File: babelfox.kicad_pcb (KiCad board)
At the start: 4 copper layers, 85.1 x 56 mm, 43 parts, among them J1 DCIN, J2 Battery, J3 GPIO, J4 Qwiic, J5 RJ45_Bel_SI-60062-F, J6 LoRA 900 SMA, J7 LoRA 2.4G ANT, J8 Cellular Ant, J9 LoRA 900 u.FL, Q1 FZ788B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

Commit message: board cleanup, add images
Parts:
- moved R9 6.23 mm to (160.6, 79.8), turned to -90 degrees
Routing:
- net BAT_Vcc: track 54.1 -> 64.1 mm
- net ADC1: track 11.6 -> 15.4 mm
- net 3v3: track 9.68 -> 12.4 mm
- net GND: vias 23 -> 24
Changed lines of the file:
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@@
 	(footprint "Resistor_SMD:R_0805_2012Metric_Pad1.20x1.40mm_HandSolder"
 		(layer "F.Cu")
-		(at 164.1856 84.8868 90)
+		(at 160.6296 79.772 -90)
 		(descr "Resistor SMD 0805 (2012 Metric), square (rectangular) end terminal, IPC_7351 nominal with elongated pad for handsoldering. (Body size source: IPC-SM-782 page 72, https://www.pcb-3d.com/wordpress/wp-content/uploads/ipc-sm-782a_amendment_1_and_2.pdf), generated with kicad-footprint-generator")
 		(tags "resistor handsolder")
 		(property "Reference" "R9"
-			(at 2.4892 0 180)
+			(at -2.5052 -0.0508 360)
 			(layer "F.SilkS")
 			(effects
@@
 		)
 		(property "Footprint" "Resistor_SMD:R_0805_2012Metric_Pad1.20x1.40mm_HandSolder"
-			(at 0 0 90)
+			(at 0 0 -90)
 			(unlocked yes)
 			(layer "F.Fab")
@@
 		)
 		(property "Datasheet" ""
-			(at 0 0 90)
+			(at 0 0 -90)
 			(unlocked yes)
 			(layer "F.Fab")
@@
 		)
 		(property "Description" "Resistor"
-			(at 0 0 90)
+			(at 0 0 -90)
 			(unlocked yes)
 			(layer "F.Fab")
@@
 		(attr smd)
 		(fp_line
-			(start -0.227064 -0.735)
-			(end 0.227064 -0.735)
+			(start -0.227064 0.735)
+			(end 0.227064 0.735)
 			(stroke
 				(width 0.12)
@@
 		)
 		(fp_line
-			(start -0.227064 0.735)
-			(end 0.227064 0.735)
+			(start -0.227064 -0.735)
+			(end 0.227064 -0.735)
 			(stroke
 				(width 0.12)
@@
 		)
 		(fp_line
-			(start 1.85 -0.95)
-			(end 1.85 0.95)
+			(start -1.85 0.95)
+			(end -1.85 -0.95)
 			(stroke
 				(width 0.05)
@@
 		)
 		(fp_line
-			(start -1.85 -0.95)
-			(end 1.85 -0.95)
+			(start 1.85 0.95)
+			(end -1.85 0.95)
 			(stroke
 				(width 0.05)
@@
 		)
 		(fp_line
-			(start 1.85 0.95)
-			(end -1.85 0.95)
+			(start -1.85 -0.95)
+			(end 1.85 -0.95)
 			(stroke
 				(width 0.05)
@@
 		)
 		(fp_line
-			(start -1.85 0.95)
-			(end -1.85 -0.95)
+			(start 1.85 -0.95)
+			(end 1.85 0.95)
 			(stroke
 				(width 0.05)
@@
 		)
 		(fp_line
-			(start 1 -0.625)
-			(end 1 0.625)
+			(start -1 0.625)
+			(end -1 -0.625)
 			(stroke
 				(width 0.1)
@@
 		)
 		(fp_line
-			(start -1 -0.625)
-			(end 1 -0.625)
+			(start 1 0.625)
+			(end -1 0.625)
 			(stroke
 				(width 0.1)
@@
 		)
 		(fp_line
-			(start 1 0.625)
-			(end -1 0.625)
+			(start -1 -0.625)
+			(end 1 -0.625)
 			(stroke
 				(width 0.1)
@@
 		)
 		(fp_line
-			(start -1 0.625)
-			(end -1 -0.625)
+			(start 1 -0.625)
+			(end 1 0.625)
 			(stroke
 				(width 0.1)
@@
 		)
 		(pad "1" smd roundrect
-			(at -1 0 90)
+			(at -1 0 270)
 			(size 1.2 1.4)
 			(layers "F.Cu" "F.Paste" "F.Mask")
@@
 		)
 		(pad "2" smd roundrect
-			(at 1 0 90)
+			(at 1 0 270)
 			(size 1.2 1.4)
 			(layers "F.Cu" "F.Paste" "F.Mask")
@@
 	)
 	(via
+		(at 163.2712 103.7336)
+		(size 0.6)
+		(drill 0.3)
+		(layers "F.Cu" "B.Cu")
+		(free yes)
+		(net 2)
+	)
+	(via
 		(at 175.8188 103.5812)
 		(size 0.6)
@@
 	)
 	(segment
+		(start 115.083 97.8408)
+		(end 116.4629 97.8408)
+		(width 0.4)
+		(layer "F.Cu")
+		(net 3)
+	)
+	(segment
 		(start 162.7124 115.9444)
 		(end 161.3728 115.9444)
@@
 	)
 	(segment
+		(start 116.4629 97.8408)
+		(end 116.6153 97.9932)
+		(width 0.4)
+		(layer "F.Cu")
+		(net 3)
+	)
+	(segment
 		(start 150.368 83.2104)
 		(end 150.368 83.1988)
@@
 		(net 3)
 	)
+	(segment
+		(start 116.5744 95.6564)
+		(end 117.6744 95.6564)
+		(width 0.4)
+		(layer "F.Cu")
+		(net 3)
+	)
 	(via
 		(at 154.7368 128.1176)
@@
 	)
 	(segment
-		(start 164.3032 86.0044)
-		(end 164.1856 85.8868)
-		(width 0.2)
-		(layer "F.Cu")
-		(net 4)
-	)
-	(segment
 		(start 168.830999 92.992201)
 		(end 168.656 93.1672)
@@
 	)
 	(segment
-		(start 165.4048 86.0044)
-		(end 164.3032 86.0044)
+		(start 161.258 78.772)
+		(end 162.1028 77.9272)
+		(width 0.2)
+		(layer "F.Cu")
+		(net 4)
+	)
+	(segment
+		(start 160.6296 78.772)
+		(end 161.258 78.772)
 		(width 0.2)
 		(layer "F.Cu")
@@
 	)
 	(via
-		(at 165.4048 86.0044)
+		(at 162.1028 77.9272)
 		(size 0.6)
 		(drill 0.3)
@@
 	)
 	(segment
-		(start 166.1682 86.0044)
-		(end 165.4048 86.0044)
+		(start 161.623327 81.459527)
+		(end 167.1842 87.0204)
 		(width 0.2)
 		(layer "B.Cu")
@@
 	)
 	(segment
+		(start 162.1028 77.9272)
+		(end 161.623327 78.406673)
+		(width 0.2)
+		(layer "B.Cu")
+		(net 4)
+	)
+	(segment
 		(start 167.6908 87.527)
-		(end 166.1682 86.0044)
+		(end 167.1842 87.0204)
 		(width 0.2)
 		(layer "B.Cu")
@@
 	)
 	(segment
+		(start 161.623327 78.406673)
+		(end 161.623327 81.459527)
+		(width 0.2)
+		(layer "B.Cu")
+		(net 4)
+	)
+	(segment
 		(start 112.914763 91.8064)
 		(end 113.1244 91.8064)
@@
 	)
 	(segment
+		(start 162.6456 82.3468)
+		(end 160.6296 82.3468)
+		(width 0.2)
+		(layer "F.Cu")
+		(net 12)
+	)
+	(segment
+		(start 160.6296 82.3468)
+		(end 160.6296 83.8868)
+		(width 0.2)
+		(layer "F.Cu")
+		(net 12)
+	)
+	(segment
 		(start 166.0048 88.173)
 		(end 166.0048 85.706)
@@
 	)
 	(segment
-		(start 164.1856 83.8868)
-		(end 160.6296 83.8868)
+		(start 160.6296 80.772)
+		(end 160.6296 82.3468)
 		(width 0.2)
 		(layer "F.Cu")
@@
 	(segment
 		(start 166.0048 85.706)
-		(end 164.1856 83.8868)
+		(end 162.6456 82.3468)
 		(width 0.2)
 		(layer "F.Cu")
@@
 	)
 	(segment
-		(start 128.7692 90.2716)
-		(end 128.7554 90.2578)
-		(width 0.2)
-		(layer "F.Cu")
-		(net 20)
-	)
-	(segment
 		(start 130.3528 90.2716)
 		(end 129.6876 89.6064)
@@
 		(net 20)
 	)
-	(segment
-		(start 129.2214 90.207)
-		(end 129.2352 90.2208)
-		(width 0.2)
-		(layer "F.Cu")
-		(net 20)
-	)
 	(via
 		(at 130.3528 90.2716)
@@
 		(net 38)
 	)
-	(segment
-		(start 119.4308 88.3412)
-		(end 119.430402 88.341598)
-		(width 0.2)
-		(layer "B.Cu")
-		(net 38)
-	)

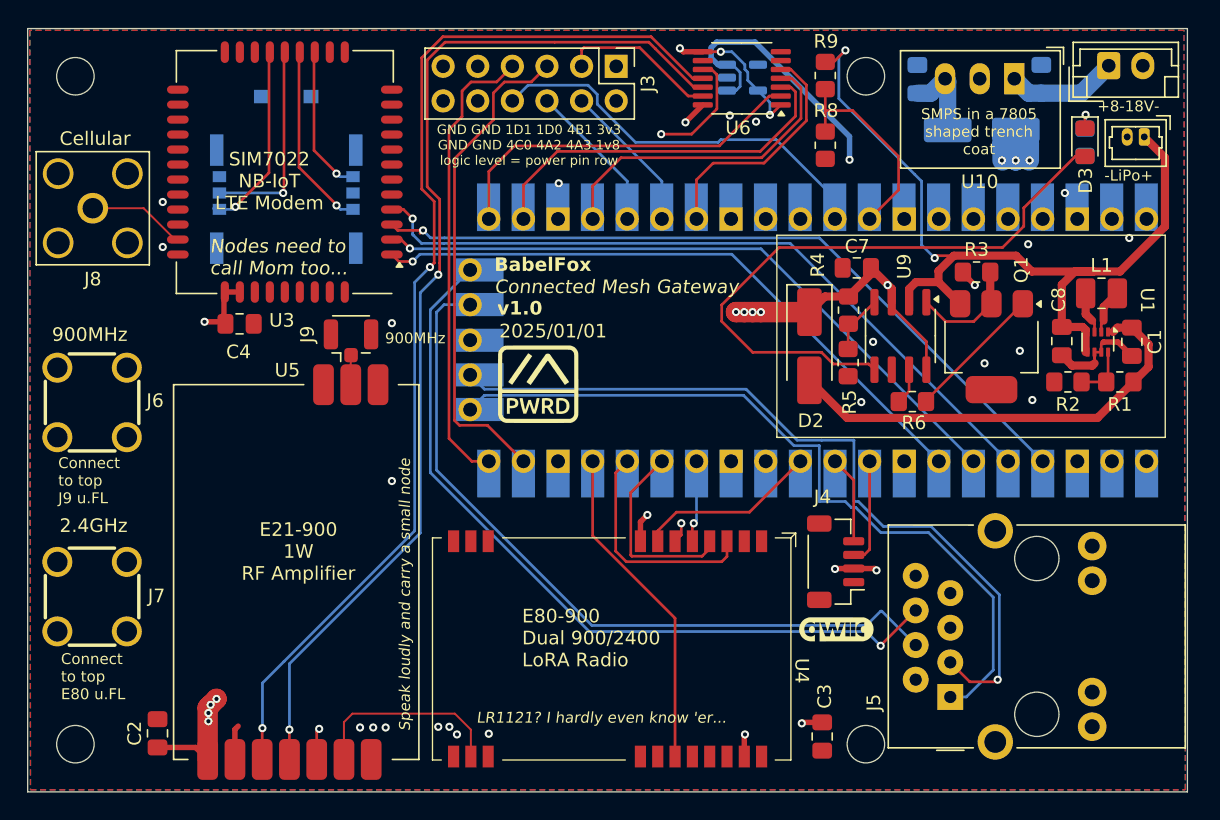
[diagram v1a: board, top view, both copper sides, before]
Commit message: neutral color logo for light/dark mode github compat
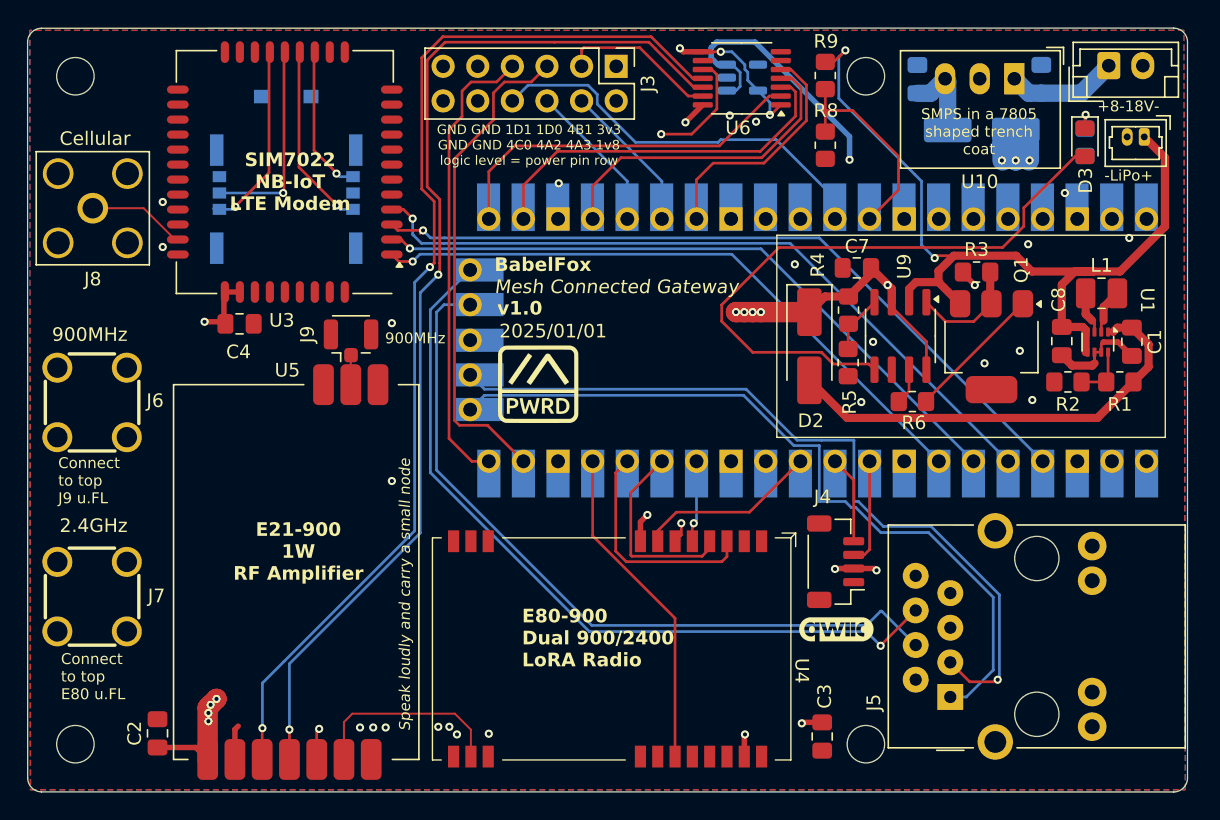
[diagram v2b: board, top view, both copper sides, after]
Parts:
- added .: LOGO, m_pwd:m_powered2, B.Cu at (130.0, 125.9)
- added .: LOGO, babelfox_logo:babelfox_logo, B.Cu at (136.7, 121.2)
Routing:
- net GND: vias 24 -> 25
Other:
- outline, holes or cut-outs redrawn
- board text added: "A connected and united human race may reach the sky, and beyond..."
- board text added: "Mesh Connected Gateway"
- board text removed: "Connected Mesh Gateway"
- board text removed: "LR1121? I hardly even know 'er..."
- board text removed: "Nodes need to call Mom too..."

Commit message: Jan 5 progress, update license to OHL-S
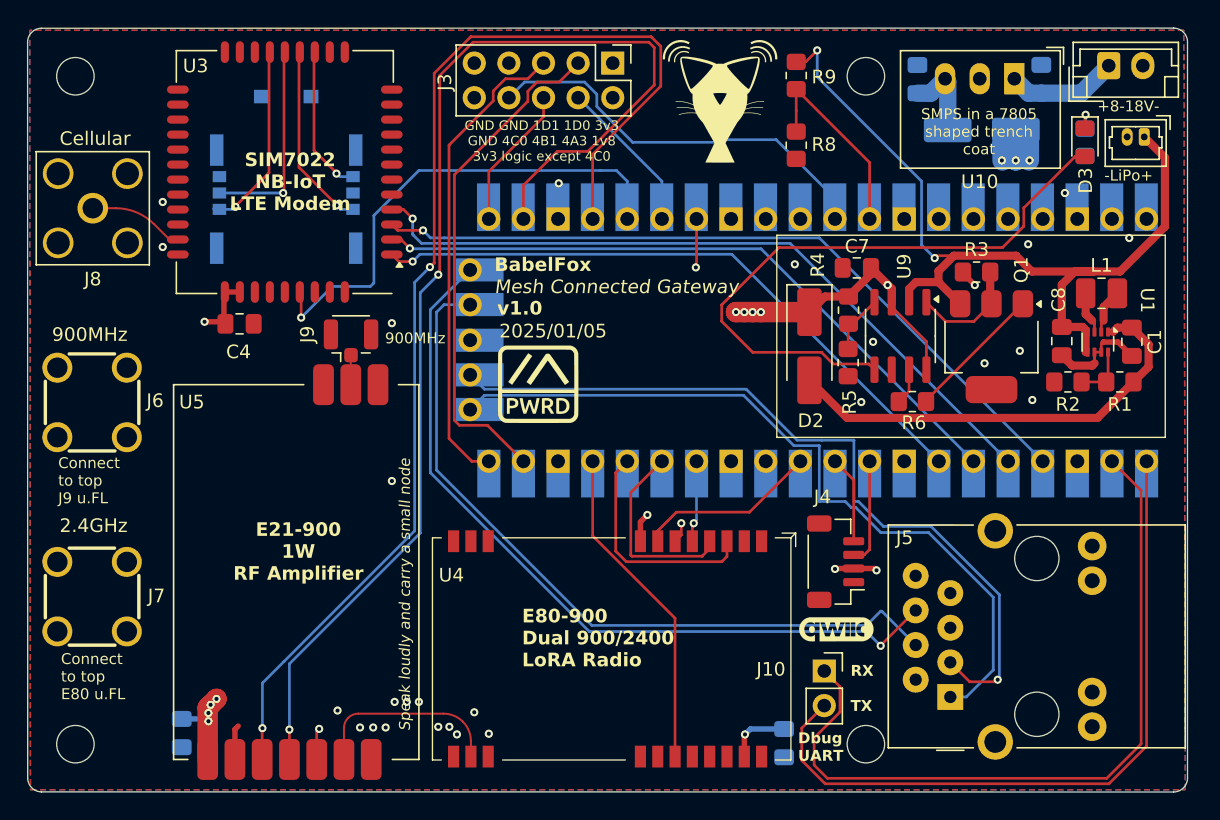
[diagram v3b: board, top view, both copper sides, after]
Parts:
- removed U6: ~, Package_SO:TSSOP-14_4.4x5mm_P0.65mm
- removed U7: TLV70018, Package_TO_SOT_SMD:SOT-23-5
- added .: LOGO, babelfox_logo:babelfox_logo_9x9, F.Cu at (152.9, 81.7)
- added J10: Debug UART, Connector_PinSocket_2.54mm:PinSocket_1x02_P2.54mm_Vertical, F.Cu at (160.6, 123.5)
- C2, C3: moved to B.Cu
- J3: footprint Connector_PinHeader_2.54mm:PinHeader_2x06_P2.54mm_Vertical -> Connector_PinHeader_2.54mm:PinHeader_2x05_P2.54mm_Vertical
- moved C3 2.84 mm to (157.6, 128.8)
- moved R8 2.13 mm to (158.5, 84.9)
- moved R9 2.13 mm to (158.5, 79.8)
- moved C2 1.78 mm to (113.4, 128.0), turned to -90 degrees
- moved J3 0.35 mm to (145.0, 78.9)
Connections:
- J3 pad 2: 1v8 -> 3v3
- J3 pad 3: GPIO0 -> UART3_TX
- J3 pad 5: UART3_TX -> UART3_RX
- J3 pad 6: GPIO3 -> GPIO0
- J3 pad 7: UART3_RX -> GND
- U2 pad 21: GPIO0_1v8 -> GPIO0
- U2 pad 22: RXEN_1v8 -> LNA_RXEN
- U2 pad 24: TXEN_1v8 -> LNA_TXEN
- U2 pad 25: GPIO3 -> LTE_WAKEUP
- U2 pad 27: LORA_IRQ_1v8 -> LORA_IRQ
- U3 pad 39: unconnected-(U3-WAKEUP-Pad39) -> LTE_WAKEUP
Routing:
- net DBUG_RX: track 0.00 -> 55.2 mm
- net DBUG_TX: track 0.00 -> 52.8 mm
- net LTE_WAKEUP: track 0.00 -> 36.3 mm, vias 0 -> 1
- net RXEN_1v8: track 27.5 -> 0.00 mm
- net GPIO0_1v8: track 27.2 -> 0.00 mm
- net TXEN_1v8: track 23.8 -> 0.00 mm
- net 5Vcc: track 183.9 -> 161.6 mm, vias 14 -> 13
- net LORA_IRQ_1v8: track 17.7 -> 0.00 mm
- net 1v8: track 17.1 -> 0.00 mm, vias 3 -> 0
- net LORA_IRQ: track 40.1 -> 24.3 mm
- net LNA_RXEN: track 78.4 -> 89.5 mm
- net GPIO3: track 11.1 -> 0.00 mm
- net LNA_TXEN: track 79.6 -> 88.3 mm
- net GPIO0: track 11.6 -> 10.6 mm
- net UART3_RX: track 33.9 -> 35.0 mm
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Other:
- board text added: "2025/01/05"
- board text added: "Dbug UART"
- board text added: "GND GND 1D1 1D0 3v3 GND 4C0 4B1 4A3 1v8 3v3 logic except 4C0"
- board text added: "RX TX"
- board text removed: "2025/01/01"
- board text removed: "GND GND 1D1 1D0 4B1 3v3 GND GND 4C0 4A2 4A3 1v8 logic level = power pin row"

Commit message: LCSC inductor... but i'm not doing LCSC anymore
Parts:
- added REF**: OSHW-Logo2_7.3x6mm_SilkScreen, Symbol:OSHW-Logo2_7.3x6mm_SilkScreen, F.Cu at (146.3, 102.4)

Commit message: board as sent to JLC 1/11
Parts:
- U1: value ~ -> TPS631000
- U3: value ~ -> SIM7022
- U4: value ~ -> E80-900M2213S
- U5: value ~ -> E21-900G30S
- U9: value ~ -> BQ2057CSNTR
- moved R2 5.22 mm to (177.7, 97.1), turned to 90 degrees
- moved L1 5.02 mm to (184.2, 99.6), turned to -90 degrees
- moved R1 4.76 mm to (177.7, 100.9), turned to 90 degrees
- moved C8 3.75 mm to (180.7, 96.6), turned to 180 degrees
- moved C1 3.52 mm to (180.6, 101.8), turned to 180 degrees
- turned U1 to 180 degrees
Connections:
- J3 pad 2: 3v3 -> 5Vcc
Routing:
- net 5Vcc: track 161.6 -> 168.0 mm
- net GND: track 14.4 -> 17.4 mm, vias 28 -> 32
- net BAT_Vcc: track 64.6 -> 62.0 mm
- net 5V_batt: track 32.8 -> 31.2 mm
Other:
- board text added: "2025/01/11"
- board text added: "GND GND 1D1 1D0 3v3 GND 4C0 4B1 4A3 5v0 3v3 logic except 4C0"
- board text removed: "2025/01/05"
- board text removed: "GND GND 1D1 1D0 3v3 GND 4C0 4B1 4A3 1v8 3v3 logic except 4C0"
